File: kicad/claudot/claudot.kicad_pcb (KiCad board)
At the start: 2 copper layers, 0 parts

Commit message: WIP
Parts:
- added C1: 30pF, Library:C_0402, F.Cu at (54.0, 48.8)
- added C10: 0.1uF, Library:C_0402, F.Cu at (66.1, 40.4)
- added C11: 0.1uF, Library:C_0402, F.Cu at (61.0, 38.2)
- added C12: 0.1uF, Library:C_0402, F.Cu at (60.0, 38.2)
- added C13: 0.1uF, Library:C_0402, F.Cu at (62.0, 49.4)
- added C14: 0.1uF, Library:C_0402, F.Cu at (59.0, 38.2)
- added C15: 10uF, Library:C_0402, F.Cu at (70.6, 38.0)
- added C16: 10uF, Library:C_0402, F.Cu at (66.0, 38.2)
- added C2: 30pF, Library:C_0402, F.Cu at (54.0, 51.1)
- added C3: 1uF, Library:C_0402, F.Cu at (65.0, 39.0)
- added C4: 1uF, Library:C_0402, F.Cu at (64.0, 39.0)
- added C5: 0.1uF, Library:C_0402, F.Cu at (55.6, 41.6)
- added C6: 0.1uF, Library:C_0402, F.Cu at (55.6, 45.4)
- added C7: 0.1uF, Library:C_0402, F.Cu at (61.0, 49.4)
- added C8: 0.1uF, Library:C_0402, F.Cu at (66.4, 46.6)
- added C9: 0.1uF, Library:C_0402, F.Cu at (66.1, 41.4)
- added D1: D_Small, Library:SOD323, F.Cu at (139.8, 57.1)
- added D10: D_Small, Library:SOD323, F.Cu at (132.6, 95.2)
- added D11: D_Small, Library:SOD323, F.Cu at (89.8, 95.2)
- added D12: D_Small, Library:SOD323, F.Cu at (54.0, 95.2)
- added D2: D_Small, Library:SOD323, F.Cu at (120.7, 57.1)
- added D3: D_Small, Library:SOD323, F.Cu at (101.7, 57.1)
- added D4: D_Small, Library:SOD323, F.Cu at (82.6, 57.1)
- added D5: D_Small, Library:SOD323, F.Cu at (56.4, 66.7)
- added D6: D_Small, Library:SOD323, F.Cu at (137.4, 76.2)
- added D7: D_Small, Library:SOD323, F.Cu at (116.0, 76.2)
- added D8: D_Small, Library:SOD323, F.Cu at (96.9, 76.2)
- added D9: D_Small, Library:SOD323, F.Cu at (77.9, 76.2)
- added F1: ASMD1206-150, Library:F_1206, F.Cu at (67.8, 34.4)
- added J1: TYPE-C-31-M-12, Library:TYPE-C-31-M-12, F.Cu at (61.9, 33.2)
- added KEY1: SW_Push, Library:CPG151101S11-16, F.Cu at (143.5, 53.3)
- added KEY10: SW_Push, Library:CPG151101S11-16, F.Cu at (136.4, 91.4)
- added KEY11: SW_Push, Library:CPG151101S11-16, F.Cu at (93.5, 91.4)
- added KEY12: SW_Push, Library:CPG151101S11-16, F.Cu at (57.8, 91.4)
- added KEY2: SW_Push, Library:CPG151101S11-16, F.Cu at (124.5, 53.3)
- added KEY3: SW_Push, Library:CPG151101S11-16, F.Cu at (105.4, 53.3)
- added KEY4: SW_Push, Library:CPG151101S11-16, F.Cu at (86.4, 53.3)
- added KEY5: SW_Push, Library:CPG151101S11-16, F.Cu at (60.2, 62.9)
- added KEY6: SW_Push, Library:CPG151101S11-16, F.Cu at (141.1, 72.4)
- added KEY7: SW_Push, Library:CPG151101S11-16, F.Cu at (119.7, 72.4)
- added KEY8: SW_Push, Library:CPG151101S11-16, F.Cu at (100.6, 72.4)
- added KEY9: SW_Push, Library:CPG151101S11-16, F.Cu at (81.6, 72.4)
- added R1: 10K, Library:R_0402, F.Cu at (63.0, 49.4)
- added R2: 1K, Library:R_0402, F.Cu at (60.0, 49.4)
- added R3: 10K, Library:R_0402, F.Cu at (55.6, 42.6)
- added R4: 1K, Library:R_0402, F.Cu at (53.7, 42.6)
- added R5: 27, Library:R_0402, F.Cu at (63.0, 38.6)
- added R6: 27, Library:R_0402, F.Cu at (62.0, 38.6)
- added R7: 5.1K, Library:R_0402, F.Cu at (63.8, 36.7)
- added R8: 5.1K, Library:R_0402, F.Cu at (59.6, 36.7)
- added REF**: MX_Switch_Stabilizer_2u, Library:MX_Switch_Stabilizer_2u, B.Cu at (59.5, 66.7)
- added REF**: MountingHole_2.2mm_M2_Pad, MountingHole:MountingHole_2.2mm_M2_Pad, B.Cu at (71.6, 98.8)
- added REF**: MX_Switch_Stabilizer_2u, Library:MX_Switch_Stabilizer_2u, B.Cu at (92.9, 95.2)
- added REF**: MountingHole_2.2mm_M2_Pad, MountingHole:MountingHole_2.2mm_M2_Pad, B.Cu at (146.4, 98.8)
- added REF**: MountingHole_2.2mm_M2_Pad, MountingHole:MountingHole_2.2mm_M2_Pad, B.Cu at (53.6, 34.6)
- added SW1: SKRP_Switch, Library:SKRP_Switch, F.Cu at (50.6, 45.9)
- added SW2: SKRP_Switch, Library:SKRP_Switch, F.Cu at (50.6, 40.2)
- added TVS-D1: SMF6V0A, Library:SMF6.0A, F.Cu at (70.0, 34.3)
- added U1: RP2040, Library:RP2040, F.Cu at (60.8, 44.2)
- added U2: W25Q16JVUXIQ, Library:W25Q16JVUXIQ, F.Cu at (56.0, 38.9)
- added U3: AP2112K-3.3, Library:SOT25, F.Cu at (68.3, 38.5)
- added Y1: 12MHz, Library:SMD3225-4P, F.Cu at (57.1, 49.9)
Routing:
- net GND: track 0.00 -> 0.84 mm, vias 0 -> 109
- net ~{RESET}: vias 0 -> 1
- net Net-(U1-QSPI_SD3): vias 0 -> 2
- net Net-(U1-QSPI_SD2): vias 0 -> 2
- net COL2: vias 0 -> 3
- net COL1: vias 0 -> 5
- net COL0: vias 0 -> 5
- net +3V3: vias 0 -> 7
- added copper zone on B.Cu, net GND
- added copper zone on F.Cu, net GND
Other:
- board outline added: 104.8 x 76.2 mm
- board text added: "1.0.0+20260117"
- board text added: "@takayoshiotake"
- board text added: "Claudot"

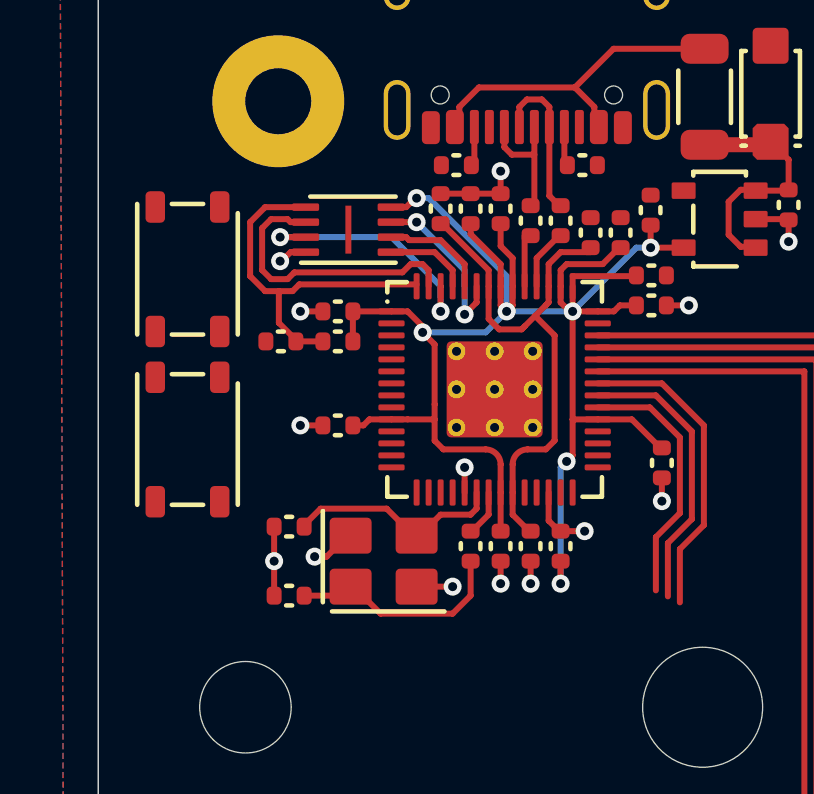
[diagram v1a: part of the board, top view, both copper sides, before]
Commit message: Add script to export latest edited KiCad deliverables
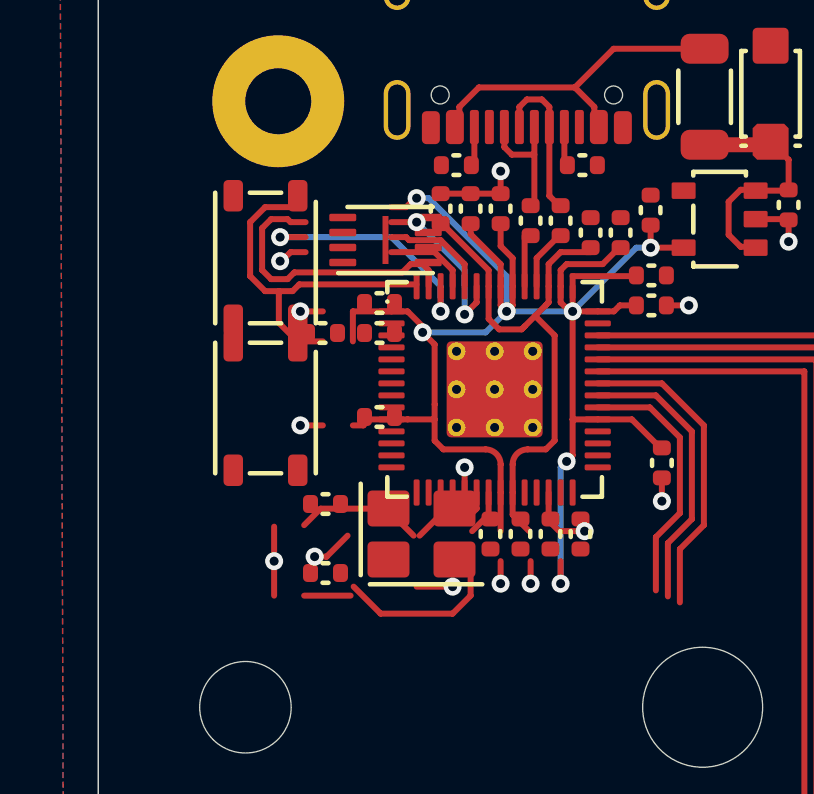
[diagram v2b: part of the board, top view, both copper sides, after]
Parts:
- moved SW1 2.80 mm to (53.2, 44.8)
- moved SW2 2.63 mm to (53.2, 39.8)
- moved Y1 1.55 mm to (58.4, 49.0)
- moved C1 1.43 mm to (55.2, 48.0)
- moved C2 1.43 mm to (55.2, 50.3)
- moved C5 1.42 mm to (57.0, 41.3)
- moved C6 1.42 mm to (57.0, 45.1)
- moved R3 1.42 mm to (57.0, 42.3)
- moved R4 1.42 mm to (55.1, 42.3)
- moved U2 1.28 mm to (57.2, 39.2)
- moved C13 0.78 mm to (62.7, 49.0)
- moved C7 0.78 mm to (61.7, 49.0)
- moved R1 0.78 mm to (63.7, 49.0)
- moved R2 0.78 mm to (60.7, 49.0)
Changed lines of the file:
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@@
 	(footprint "Library:R_0402"
 		(layer "F.Cu")
-		(at 60.0375 49.405 -90)
+		(at 60.7000 49.0000 -90)
 		(property "Reference" "R2"
 			(at 0 -1.5 270)
@@
 	(footprint "Library:C_0402"
 		(layer "F.Cu")
-		(at 61.0375 49.405 -90)
+		(at 61.7000 49.0000 -90)
 		(property "Reference" "C7"
 			(at 0 -1.5 270)
@@
 	(footprint "Library:W25Q16JVUXIQ"
 		(layer "F.Cu")
-		(at 55.9625 38.855 -90)
+		(at 57.2000 39.2000 -90)
 		(descr "https://www.winbond.com/hq/product/code-storage-flash-memory/serial-nor-flash/?__locale=ja&partNo=W25Q16JV")
 		(tags "16MBit, USON8 2x3m, C2843335")
@@
 	(footprint "Library:C_0402"
 		(layer "F.Cu")
-		(at 53.9875 51.055 180)
+		(at 55.2000 50.3000 180)
 		(property "Reference" "C2"
 			(at 0 -1.5 180)
@@
 	(footprint "Library:C_0402"
 		(layer "F.Cu")
-		(at 53.9875 48.755 180)
+		(at 55.2000 48.0000 180)
 		(property "Reference" "C1"
 			(at 0 -1.5 180)
@@
 	(footprint "Library:C_0402"
 		(layer "F.Cu")
-		(at 62.0375 49.405 -90)
+		(at 62.7000 49.0000 -90)
 		(property "Reference" "C13"
 			(at 0 -1.5 270)
@@
 	(footprint "Library:R_0402"
 		(layer "F.Cu")
-		(at 53.7125 42.58 180)
+		(at 55.1000 42.3000 180)
 		(property "Reference" "R4"
 			(at 0 -1.5 180)
@@
 	(footprint "Library:C_0402"
 		(layer "F.Cu")
-		(at 55.6125 45.38 180)
+		(at 57.0000 45.1000 180)
 		(property "Reference" "C6"
 			(at 0 -1.5 180)
@@
 	(footprint "Library:SKRP_Switch"
 		(layer "F.Cu")
-		(at 50.6 40.175 -90)
+		(at 53.2000 39.8000 -90)
 		(tags "ALPSALPINE, SKRPABE010, C115360")
 		(property "Reference" "SW2"
@@
 	(footprint "Library:C_0402"
 		(layer "F.Cu")
-		(at 55.6125 41.58 180)
+		(at 57.0000 41.3000 180)
 		(property "Reference" "C5"
 			(at 0 -1.5 180)
@@
 	(footprint "Library:R_0402"
 		(layer "F.Cu")
-		(at 63.0375 49.405 90)
+		(at 63.7000 49.0000 90)
 		(property "Reference" "R1"
 			(at 0 -1.5 90)
@@
 	(footprint "Library:SKRP_Switch"
 		(layer "F.Cu")
-		(at 50.6 45.85 -90)
+		(at 53.2000 44.8000 -90)
 		(tags "ALPSALPINE, SKRPABE010, C115360")
 		(property "Reference" "SW1"
@@
 	(footprint "Library:SMD3225-4P"
 		(layer "F.Cu")
-		(at 57.1375 49.905)
+		(at 58.4000 49.0000 0)
 		(property "Reference" "Y1"
 			(at -2.197 -2.435 0)
@@
 	(footprint "Library:R_0402"
 		(layer "F.Cu")
-		(at 55.6125 42.58 180)
+		(at 57.0000 42.3000 180)
 		(property "Reference" "R3"
 			(at 0 -1.5 180)
